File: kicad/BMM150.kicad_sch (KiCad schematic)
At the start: 3 parts, among them U1101 BMM150

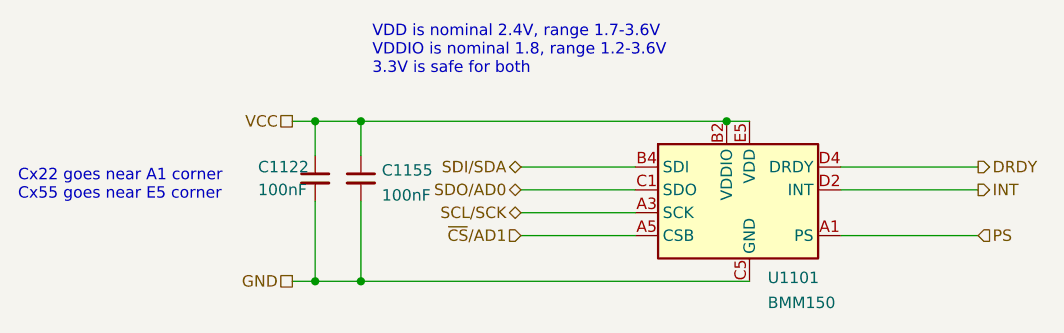
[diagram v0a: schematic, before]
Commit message: Broke down sensor block into a tree of sheets
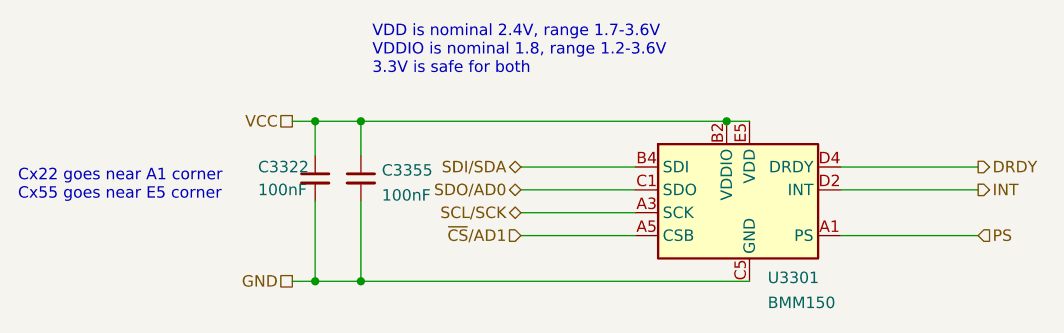
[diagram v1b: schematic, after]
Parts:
- renumbered C1122 to C3322, C1155 to C3355, U1101 to U3301
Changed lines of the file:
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@@
   (symbol (lib_id "Device:C_Small") (at 83.82 64.77 0)
     (in_bom yes) (on_board yes) (fields_autoplaced)
-    (property "Reference" "C1155" (id 0) (at 86.1441 63.8678 0)
+    (property "Reference" "C3355" (id 0) (at 86.1441 63.8678 0)
       (effects (font (size 1.27 1.27)) (justify left))
     )
@@
   (symbol (lib_id "Sensor_Magnetic:BMM150") (at 127 66.04 0)
     (in_bom yes) (on_board yes) (fields_autoplaced)
-    (property "Reference" "U1101" (id 0) (at 129.0194 75.8095 0)
+    (property "Reference" "U3301" (id 0) (at 129.0194 75.8095 0)
       (effects (font (size 1.27 1.27)) (justify left))
     )
@@
   (symbol (lib_id "Device:C_Small") (at 78.74 64.77 0)
     (in_bom yes) (on_board yes)
-    (property "Reference" "C1122" (id 0) (at 72.39 63.5 0)
+    (property "Reference" "C3322" (id 0) (at 72.39 63.5 0)
       (effects (font (size 1.27 1.27)) (justify left))
     )

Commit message: Added Digikey references
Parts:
- C3322, C3355: Digikey (none) -> 399-C0402C104K4RAC7411CT-ND
- U3301: footprint Package_CSP:WLCSP-12_1.56x1.56mm_P0.4mm -> KwanSystems:BMM150; Digikey (none) -> 828-1044-1-ND; Purpose (none) -> Magnetic sensor
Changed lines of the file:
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@@
+      (effects (font (size 1.27 1.27)) hide)
+    )
+    (property "Digikey" "399-C0402C104K4RAC7411CT-ND" (id 4) (at 83.82 64.77 0)
       (effects (font (size 1.27 1.27)) hide)
     )
@@
       (effects (font (size 1.27 1.27)) (justify left))
     )
-    (property "Footprint" "Package_CSP:WLCSP-12_1.56x1.56mm_P0.4mm" (id 2) (at 115.57 62.23 0)
+    (property "Footprint" "KwanSystems:BMM150" (id 2) (at 115.57 62.23 0)
       (effects (font (size 1.27 1.27)) hide)
     )
     (property "Datasheet" "https://www.mouser.com/datasheet/2/783/BST-BMM150-DS001-01-786480.pdf" (id 3) (at 118.11 59.69 0)
+      (effects (font (size 1.27 1.27)) hide)
+    )
+    (property "Digikey" "828-1044-1-ND" (id 4) (at 127 66.04 0)
+      (effects (font (size 1.27 1.27)) hide)
+    )
+    (property "Purpose" "Magnetic sensor" (id 5) (at 127 66.04 0)
       (effects (font (size 1.27 1.27)) hide)
     )
@@
       (effects (font (size 1.27 1.27)) hide)
     )
+    (property "Digikey" "399-C0402C104K4RAC7411CT-ND" (id 4) (at 78.74 64.77 0)
+      (effects (font (size 1.27 1.27)) hide)
+    )

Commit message: Added a purpose field to bypass capacitors
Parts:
- C3322: Purpose (none) -> BMM VDDIO bypass
- C3355: Purpose (none) -> BMM VDD bypass
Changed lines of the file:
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@@
+      (effects (font (size 1.27 1.27)) hide)
+    )
+    (property "Purpose" "BMM VDD bypass" (id 5) (at 83.82 64.77 0)
       (effects (font (size 1.27 1.27)) hide)
     )
@@
       (effects (font (size 1.27 1.27)) hide)
     )
+    (property "Purpose" "BMM VDDIO bypass" (id 5) (at 78.74 64.77 0)
+      (effects (font (size 1.27 1.27)) hide)
+    )

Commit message: Checkin before branch
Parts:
- renumbered C3322 to C1722, C3355 to C1755, U3301 to U1701
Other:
- note added: "VDD is nominal 2.4V, range 1.7-3.6V VDDIO is nominal 1.8, range 1.2-3.6V 1.8V and 3.3V is safe for both"
- note removed: "VDD is nominal 2.4V, range 1.7-3.6V VDDIO is nominal 1.8, range 1.2-3.6V 3.3V is safe for both"
- company: (none) -> Kwan Systems
- title: (none) -> Rollercoasterometer
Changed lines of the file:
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@@
 (kicad_sch (version 20211123) (generator eeschema)
-  (paper "A4")
+  (paper "USLetter")
+  (title_block
+    (title "Rollercoasterometer")
+    (date "2022-10-07")
+    (company "Kwan Systems")
+  )
   (junction (at 124.46 58.42) (diameter 0) (color 0 0 0 0)
   )
@@
     (stroke (width 0) (type default) (color 0 0 0 0))
   )
-  (text "VDD is nominal 2.4V, range 1.7-3.6V\nVDDIO is nominal 1.8, range 1.2-3.6V\n3.3V is safe for both"
+  (text "VDD is nominal 2.4V, range 1.7-3.6V\nVDDIO is nominal 1.8, range 1.2-3.6V\n1.8V and 3.3V is safe for both"
     (at 85.09 53.34 0)
     (effects (font (size 1.27 1.27)) (justify left bottom))
@@
     (effects (font (size 1.27 1.27)) (justify right))
   )
-  (symbol (lib_id "Device:C_Small") (at 83.82 64.77 0)
+  (symbol (lib_id "Device:C_Small") (at 83.82 64.77 0) (unit 1)
     (in_bom yes) (on_board yes) (fields_autoplaced)
-    (property "Reference" "C3355" (id 0) (at 86.1441 63.8678 0)
+    (property "Reference" "C1755" (id 0) (at 86.1441 63.9416 0)
       (effects (font (size 1.27 1.27)) (justify left))
     )
-    (property "Value" "100nF" (id 1) (at 86.1441 66.6429 0)
+    (property "Value" "100nF" (id 1) (at 86.1441 66.4785 0)
       (effects (font (size 1.27 1.27)) (justify left))
     )
@@
     (pin "2")
   )
-  (symbol (lib_id "Sensor_Magnetic:BMM150") (at 127 66.04 0)
+  (symbol (lib_id "Sensor_Magnetic:BMM150") (at 127 66.04 0) (unit 1)
     (in_bom yes) (on_board yes) (fields_autoplaced)
-    (property "Reference" "U3301" (id 0) (at 129.0194 75.8095 0)
+    (property "Reference" "U1701" (id 0) (at 129.0194 75.6904 0)
       (effects (font (size 1.27 1.27)) (justify left))
     )
-    (property "Value" "BMM150" (id 1) (at 129.0194 78.5846 0)
+    (property "Value" "BMM150" (id 1) (at 129.0194 78.2273 0)
       (effects (font (size 1.27 1.27)) (justify left))
     )
@@
     (pin "E5")
   )
-  (symbol (lib_id "Device:C_Small") (at 78.74 64.77 0)
+  (symbol (lib_id "Device:C_Small") (at 78.74 64.77 0) (unit 1)
     (in_bom yes) (on_board yes)
-    (property "Reference" "C3322" (id 0) (at 72.39 63.5 0)
+    (property "Reference" "C1722" (id 0) (at 72.39 63.5 0)
       (effects (font (size 1.27 1.27)) (justify left))
     )
